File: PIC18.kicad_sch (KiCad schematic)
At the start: 17 parts, among them J1 Conn_02x20_Counter_Clockwise, J2 Conn_01x06_Pin, J3 USB_A, U1 PIC18F4321-I/P, U2 LM4040DBZ-4.1, U3 FT230XS, Y1 8 MHz

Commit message: footprint and step assignment
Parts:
- removed J2: Conn_01x06_Pin, Connector_PinHeader_1.27mm:PinHeader_1x06_P1.27mm_Vertical, symbol Connector:Conn_01x06_Pin
- added J2: Conn_01x06, Connector_PinHeader_2.54mm:PinHeader_1x06_P2.54mm_Vertical, symbol Connector_Generic:Conn_01x06
- added J4: Conn_01x03, Connector_PinHeader_2.54mm:PinHeader_1x03_P2.54mm_Vertical, symbol Connector_Generic:Conn_01x03
- added J5: Conn_01x02, Connector_PinHeader_2.54mm:PinHeader_1x02_P2.54mm_Vertical, symbol Connector_Generic:Conn_01x02
- added R5: 33, Resistor_SMD:R_0402_1005Metric, symbol Device:R_US
- added R6: 220, Resistor_SMD:R_0402_1005Metric, symbol Device:R_US
- J1: footprint PinSockets:PinSocket_2x20_Counter_Clockwise_P1.27mm_Vertical -> PinSockets:PinSocket_2x20_Counter_Clockwise_P2.54mm_Vertical
- U1: footprint Package_DIP:DIP-40_W15.24mm_Socket -> DILB40P-223TLF:AMPHENOL_DILB40P-223TLF
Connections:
- net *MCLR/VPP/RE3: now also J2.1 (Pin_1)
- net GND: now also TH1.2, U2.2 (A), J2.3 (Pin_3)
- net RA1/AN1: now also J4.2 (Pin_2)
- net RA3/AN3/VREF+: now also U2.1 (K), J4.3 (Pin_3), R5.2, R6.2
- net RB6/KBI2/PGC: now also J2.5 (Pin_5)
- net RB7/KBI3/PGD: now also J2.4 (Pin_4)
- net RC6/TX/CK: now also U3.4 (RXD); no longer U3.1 (TXD)
- net RC7/RX/DT: now also U3.1 (TXD); no longer U3.4 (RXD)
- net VCC: now also J2.2 (Pin_2), R5.1
- net VTHERM: now reaches TH1.1
- net VTHERM: now also J5.1 (Pin_1), J5.2 (Pin_2), R6.1
- no-connect marks 1 -> 2
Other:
- note added: "Voltage Ref"
- moved on the sheet: R1, TH1, U2

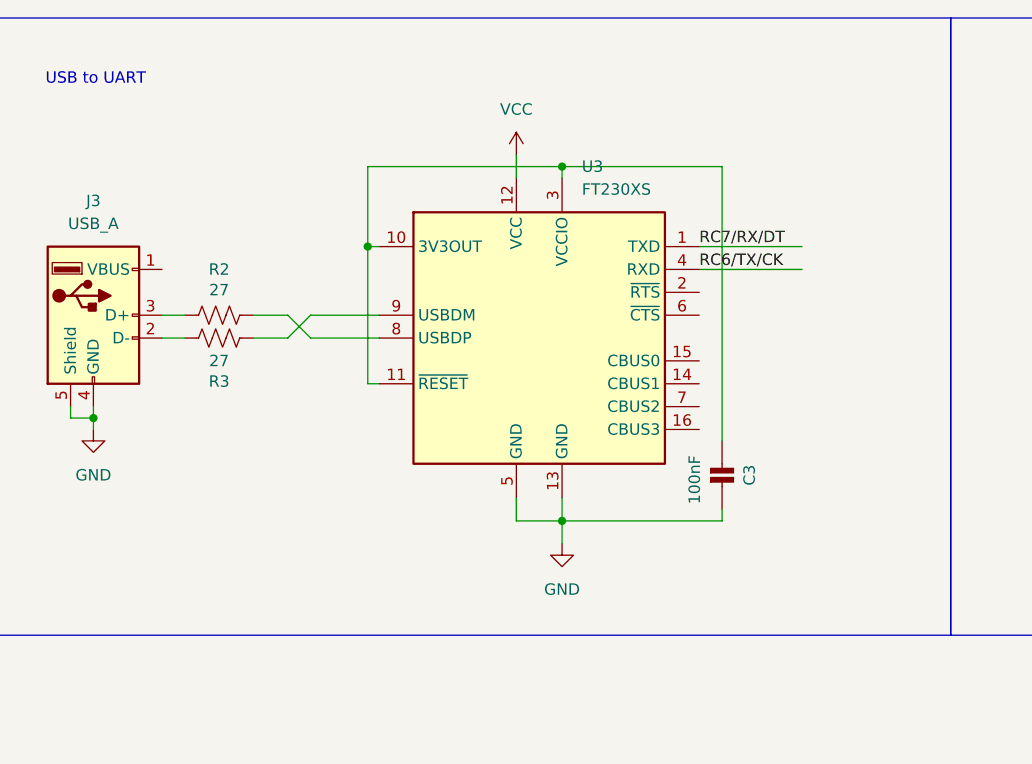
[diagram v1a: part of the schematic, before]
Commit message: More footprint assignments
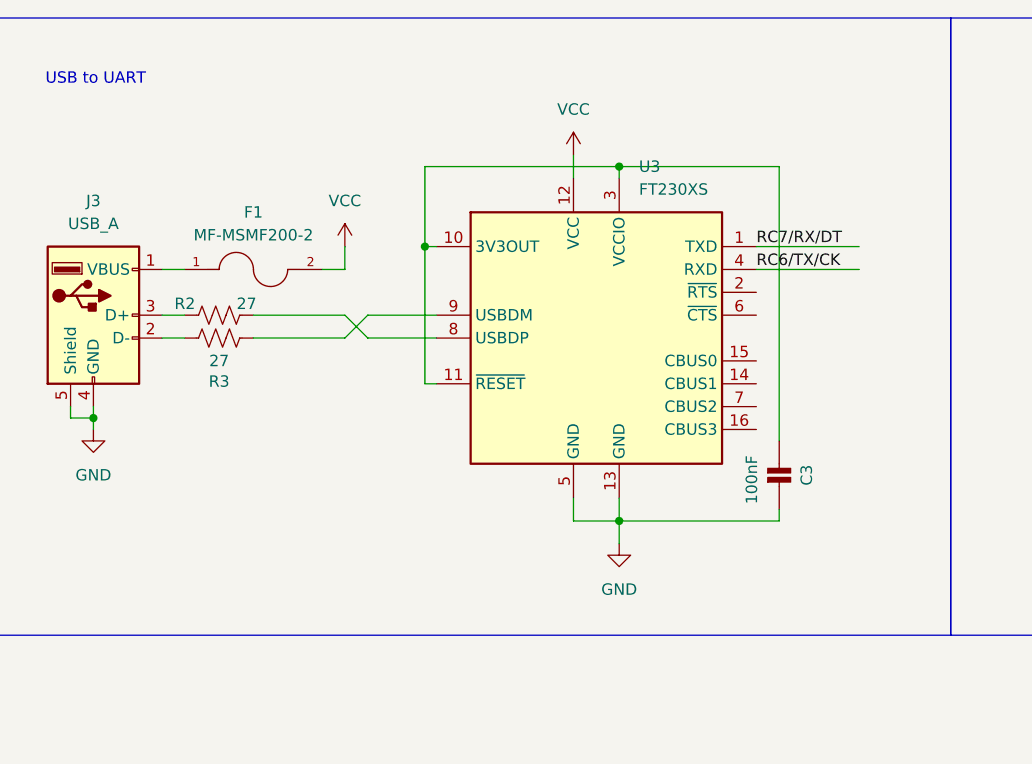
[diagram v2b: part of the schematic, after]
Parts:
- added F1: MF-MSMF200-2, MF-MSMF200-2:FUSER_MF-MSMF200-2, symbol MF-MSMF200-2:MF-MSMF200-2
- J3: footprint Connector_USB:USB_A_Molex_67643_Horizontal -> ul_676433910:CONN_67643-3910_MOL
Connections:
- net VCC: now also F1.2
- net at J3.1 (VBUS): now also F1.1
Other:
- moved on the sheet: C3, U3

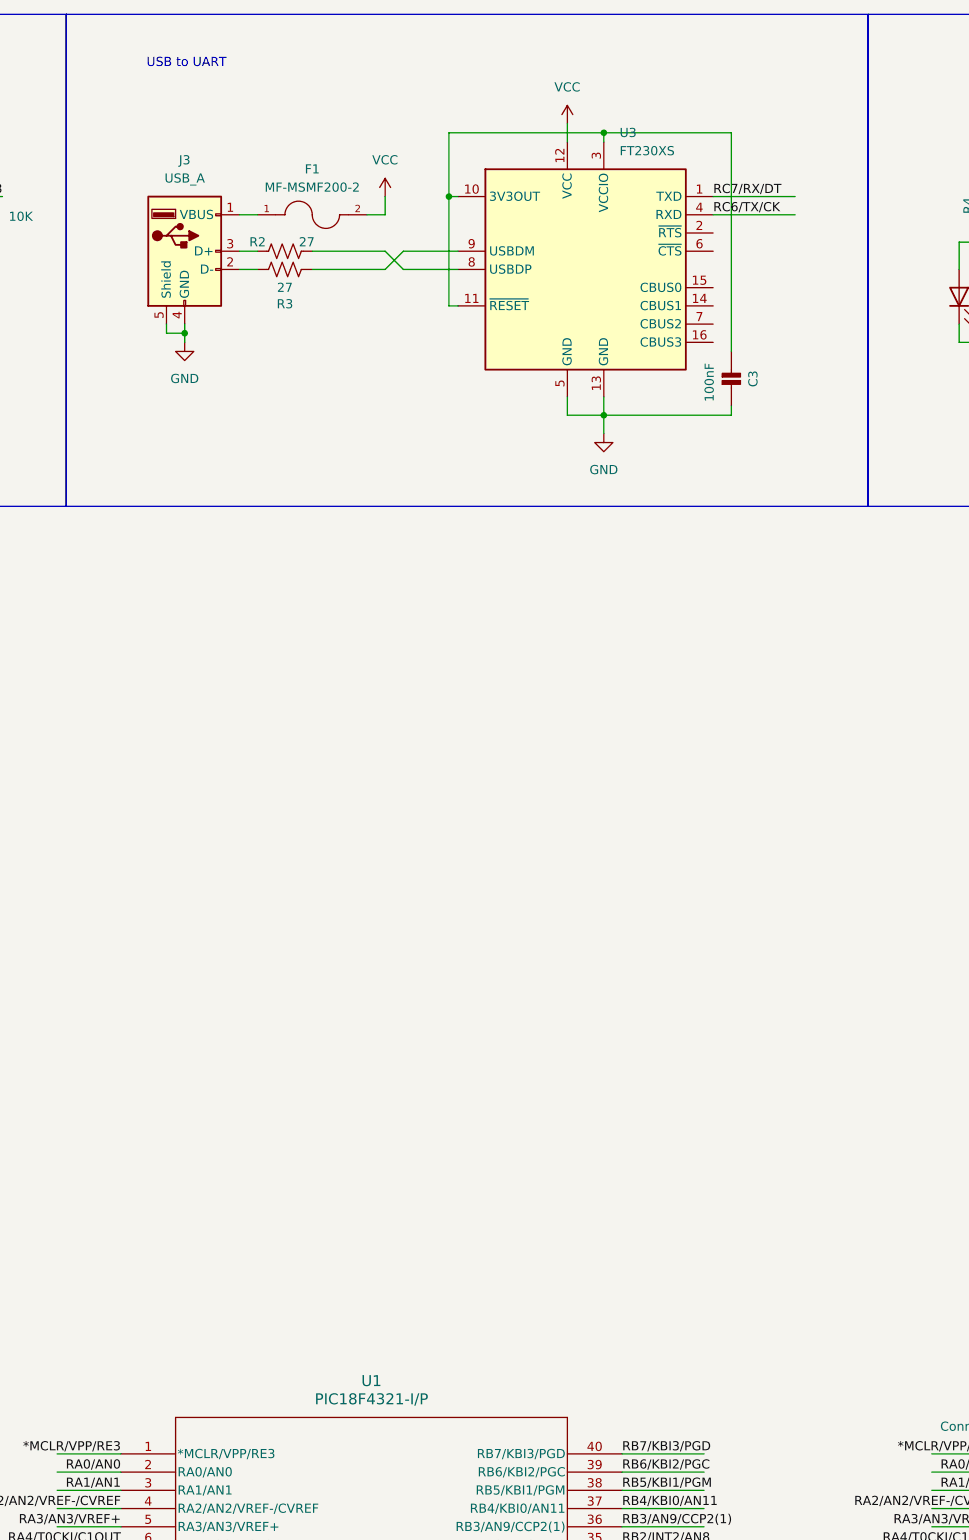
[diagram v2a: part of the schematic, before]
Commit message: yet more footprint assignment
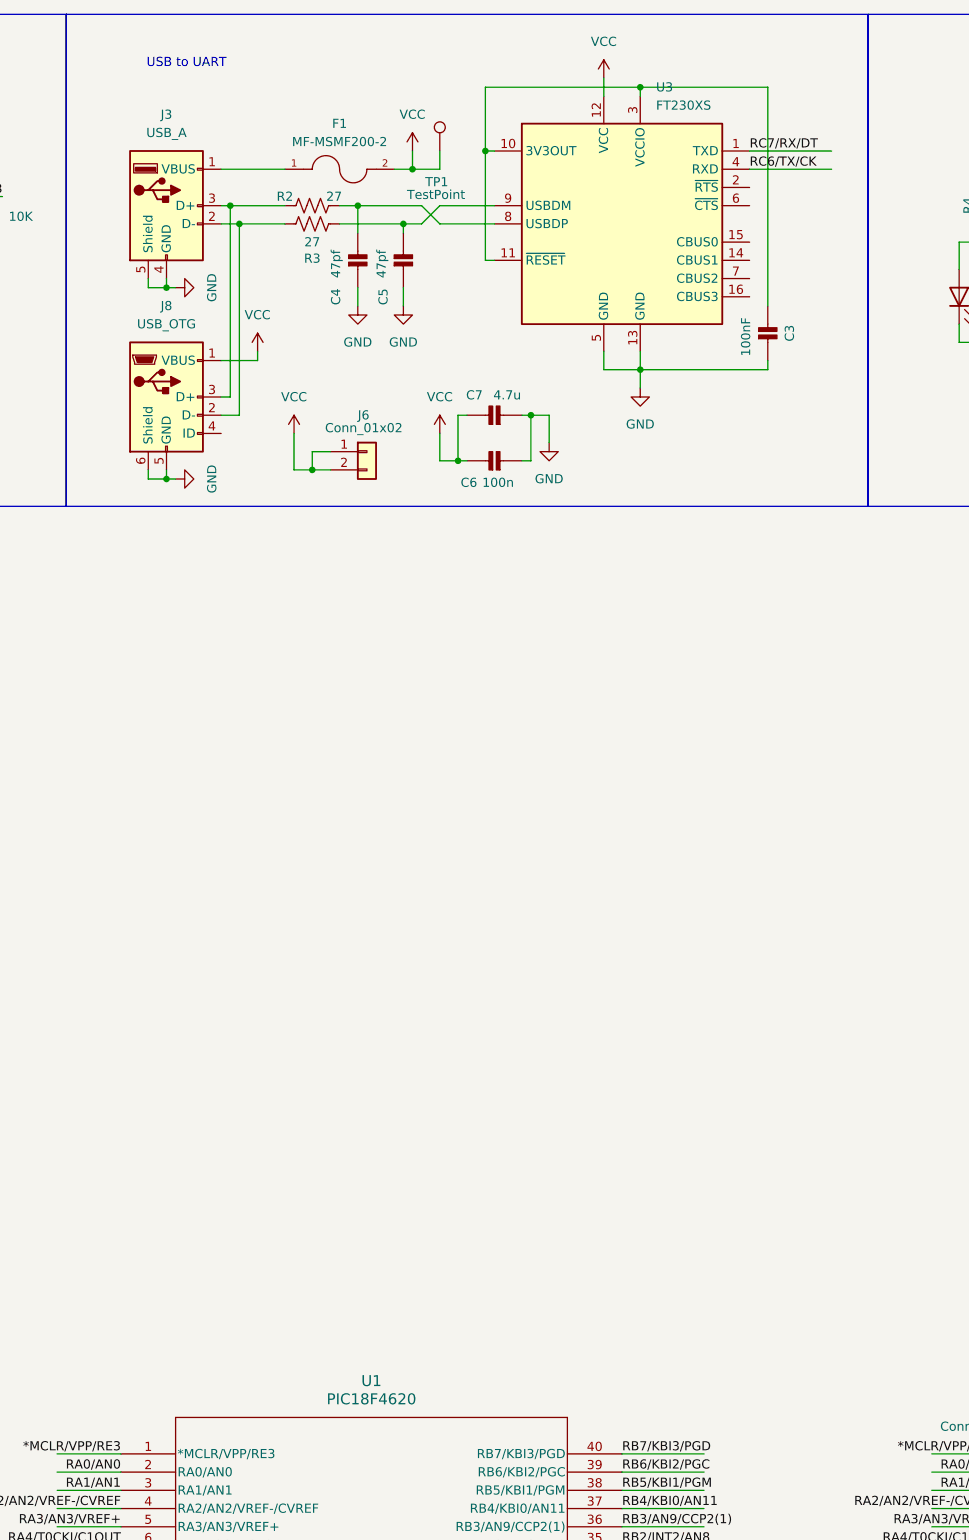
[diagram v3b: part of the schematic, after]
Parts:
- added C4, C5: 47pf, Capacitor_SMD:C_0402_1005Metric, symbol Adafruit ItsyBitsy RP2040-eagle-import:CAP_CERAMIC_0402NO
- added C6: 100n, Capacitor_SMD:C_0402_1005Metric, symbol Adafruit ItsyBitsy RP2040-eagle-import:CAP_CERAMIC_0402NO
- added C7: 4.7u, Capacitor_SMD:C_0402_1005Metric, symbol Adafruit ItsyBitsy RP2040-eagle-import:CAP_CERAMIC_0402NO
- added J6: Conn_01x02, Connector_PinHeader_2.54mm:PinHeader_1x02_P2.54mm_Vertical, symbol Connector_Generic:Conn_01x02
- added J8: USB_OTG, Connector_USB:USB_Mini-B_Lumberg_2486_01_Horizontal, symbol Connector:USB_OTG
- added TP1: TestPoint, TestPoint:TestPoint_Pad_D2.5mm, symbol Connector:TestPoint
- J3: footprint ul_676433910:CONN_67643-3910_MOL -> Connector_USB:USB_A_TE_292303-7_Horizontal
- U1: value PIC18F4321-I/P -> PIC18F4620
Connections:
- net GND: now also C4.2, C5.2, C6.2, C7.2, J8.5 (GND), J8.6 (Shield)
- net VCC: now also C6.1, C7.1, J6.1 (Pin_1), J6.2 (Pin_2), J8.1 (VBUS), TP1.1
- net at J3.2 (D-), R3.1: now also J8.2 (D-)
- net at J3.3 (D+), R2.1: now also J8.3 (D+)
- net at R3.2, U3.9 (USBDM): now also C5.1
- net at R2.2, U3.8 (USBDP): now also C4.1
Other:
- moved on the sheet: C3, F1, J3, R2, R3, U3

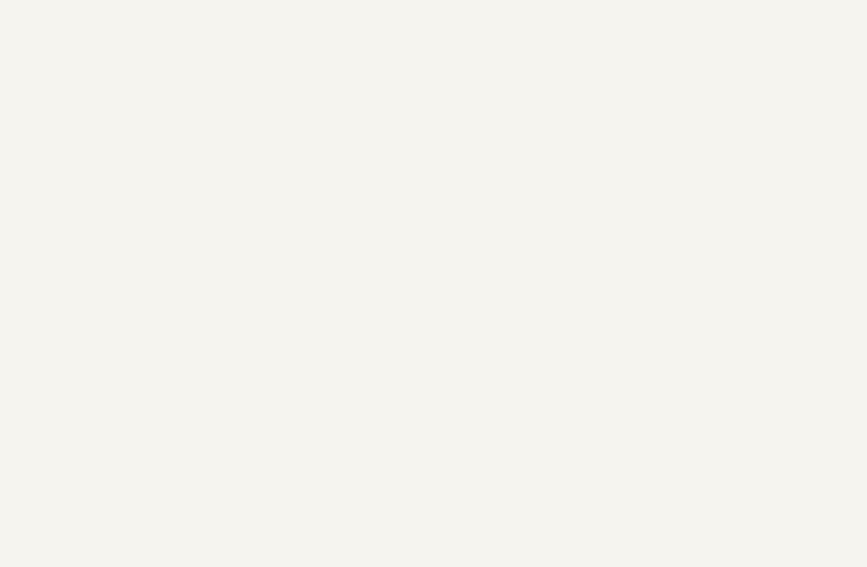
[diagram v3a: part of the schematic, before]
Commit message: added Zener and colored pin headers
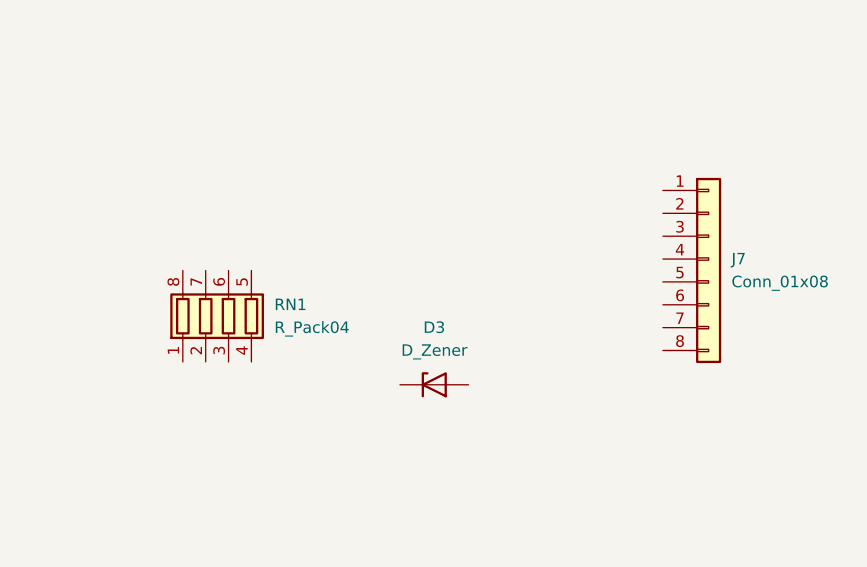
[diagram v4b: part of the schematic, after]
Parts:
- added D3: D_Zener, ZM4748A_L0G:DIOMELF5124N, symbol Device:D_Zener
- added J7: Conn_01x08, Connector_PinHeader_2.54mm:PinHeader_2x04_P2.54mm_Vertical, symbol Connector_Generic:Conn_01x08
- added RN1: R_Pack04, Resistor_SMD:R_Array_Convex_4x0603, symbol Device:R_Pack04
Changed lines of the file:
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@@
+	)
+	(symbol
+		(lib_id "Connector_Generic:Conn_01x08")
+		(at 292.1 114.3 0)
+		(unit 1)
+		(exclude_from_sim no)
+		(in_bom yes)
+		(on_board yes)
+		(dnp no)
+		(fields_autoplaced yes)
+		(property "Reference" "J7"
+			(at 294.64 114.2999 0)
+			(effects
+				(font
+					(size 1.27 1.27)
+				)
+				(justify left)
+			)
+		)
+		(property "Value" "Conn_01x08"
+			(at 294.64 116.8399 0)
+			(effects
+				(font
+					(size 1.27 1.27)
+				)
+				(justify left)
+			)
+		)
+		(property "Footprint" "Connector_PinHeader_2.54mm:PinHeader_2x04_P2.54mm_Vertical"
+			(at 292.1 114.3 0)
+			(effects
+				(font
+					(size 1.27 1.27)
+				)
+				(hide yes)
+			)
+		)
+		(property "Datasheet" "~"
+			(at 292.1 114.3 0)
+			(effects
+				(font
+					(size 1.27 1.27)
+				)
+				(hide yes)
+			)
+		)
+		(property "Description" "Generic connector, single row, 01x08, script generated (kicad-library-utils/schlib/autogen/connector/)"
+			(at 292.1 114.3 0)
+			(effects
+				(font
+					(size 1.27 1.27)
+				)
+				(hide yes)
+			)
+		)
+		(pin "3"
+		)
+		(pin "4"
+		)
+		(pin "1"
+		)
+		(pin "8"
+		)
+		(pin "5"
+		)
+		(pin "6"
+		)
+		(pin "2"
+		)
+		(pin "7"
+		)
+		(instances
+			(project "PIC18"
+				(path "/e4a6b067-3b9b-4409-bea0-0b6131f207b6"
+					(reference "J7")
+					(unit 1)
+				)
+			)
+		)
 	)
 	(symbol
@@
 	)
 	(symbol
+		(lib_id "Device:D_Zener")
+		(at 261.62 128.27 0)
+		(unit 1)
+		(exclude_from_sim no)
+		(in_bom yes)
+		(on_board yes)
+		(dnp no)
+		(fields_autoplaced yes)
+		(property "Reference" "D3"
+			(at 261.62 121.92 0)
+			(effects
+				(font
+					(size 1.27 1.27)
+				)
+			)
+		)
+		(property "Value" "D_Zener"
+			(at 261.62 124.46 0)
+			(effects
+				(font
+					(size 1.27 1.27)
+				)
+			)
+		)
+		(property "Footprint" "ZM4748A_L0G:DIOMELF5124N"
+			(at 261.62 128.27 0)
+			(effects
+				(font
+					(size 1.27 1.27)
+				)
+				(hide yes)
+			)
+		)
+		(property "Datasheet" "~"
+			(at 261.62 128.27 0)
+			(effects
+				(font
+					(size 1.27 1.27)
+				)
+				(hide yes)
+			)
+		)
+		(property "Description" "Zener diode"
+			(at 261.62 128.27 0)
+			(effects
+				(font
+					(size 1.27 1.27)
+				)
+				(hide yes)
+			)
+		)
+		(pin "1"
+		)
+		(pin "2"
+		)
+		(instances
+			(project "PIC18"
+				(path "/e4a6b067-3b9b-4409-bea0-0b6131f207b6"
+					(reference "D3")
+					(unit 1)
+				)
+			)
+		)
+	)
+	(symbol
 		(lib_id "power:GND")
 		(at 139.7 64.77 0)
@@
 					(unit 1)
 				)
+			)
+		)
+	)
+	(symbol
+		(lib_id "Device:R_Pack04")
+		(at 238.76 120.65 0)
+		(unit 1)
+		(exclude_from_sim no)
+		(in_bom yes)
+		(on_board yes)
+		(dnp no)
+		(fields_autoplaced yes)
+		(property "Reference" "RN1"
+			(at 243.84 119.3799 0)
+			(effects
+				(font
+					(size 1.27 1.27)
+				)
+				(justify left)
+			)
+		)
+		(property "Value" "R_Pack04"
+			(at 243.84 121.9199 0)
+			(effects
+				(font
+					(size 1.27 1.27)
+				)
+				(justify left)
+			)
+		)
+		(property "Footprint" "Resistor_SMD:R_Array_Convex_4x0603"
+			(at 245.745 120.65 90)
+			(effects
+				(font
+					(size 1.27 1.27)
+				)
+				(hide yes)
+			)
+		)
+		(property "Datasheet" "~"
+			(at 238.76 120.65 0)
+			(effects
+				(font
+					(size 1.27 1.27)
+				)
+				(hide yes)
+			)
+		)
+		(property "Description" "4 resistor network, parallel topology"
+			(at 238.76 120.65 0)
+			(effects
+				(font
+					(size 1.27 1.27)
+				)
+				(hide yes)
+			)
+		)
+		(pin "1"
+		)
+		(pin "3"
+		)
+		(pin "8"
+		)
+		(pin "2"
+		)
+		(pin "6"
+		)
+		(pin "5"
+		)
+		(pin "7"
+		)
+		(pin "4"
+		)
+		(instances
+			(project "PIC18"
+				(path "/e4a6b067-3b9b-4409-bea0-0b6131f207b6"
+					(reference "RN1")
+					(unit 1)
+				)
